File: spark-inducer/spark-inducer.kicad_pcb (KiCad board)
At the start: 2 copper layers, 233.3 x 128.5 mm, 100 parts, among them J1 Eurorack_Power_Header, J10 IO_A_1, J11 IO_A_3, J12 IO_A_2, J13 IO_A_4, J14 IO_B_1, J15 IO_B_3, J16 IO_B_2, J17 IO_B_4, J18 REF_SELECT, J19 POWER_A_1, J2 IO1, J20 POWER_A_2, J21 POWER_A_3, J22 POWER_A_4, J23 POWER_B_1, J24 POWER_B_2, J25 POWER_B_3, J26 POWER_B_4, J3 IO2, J4 IO3, J5 IO4, J6 IO5, J7 IO6, J8 OUT1, J9 OUT2, SW1 SWITCH, U1 TL072B, U2 TL072B, U3 TL431B, U4 L78LXX, U5 LM4040, U6 REF50XX

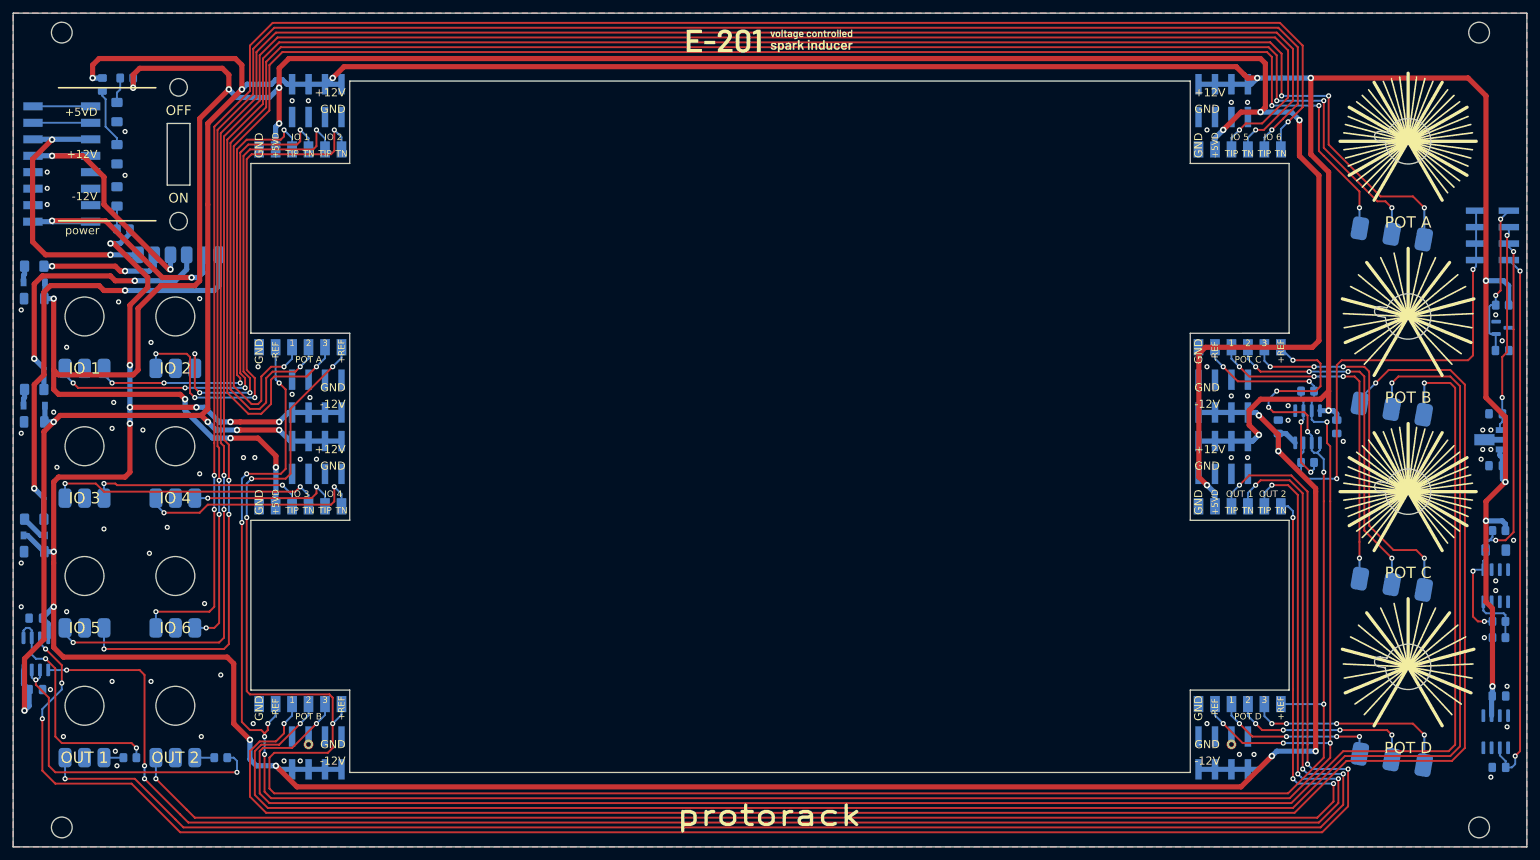
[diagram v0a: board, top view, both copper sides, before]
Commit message: Fix breadboard spacings, Add glue marks
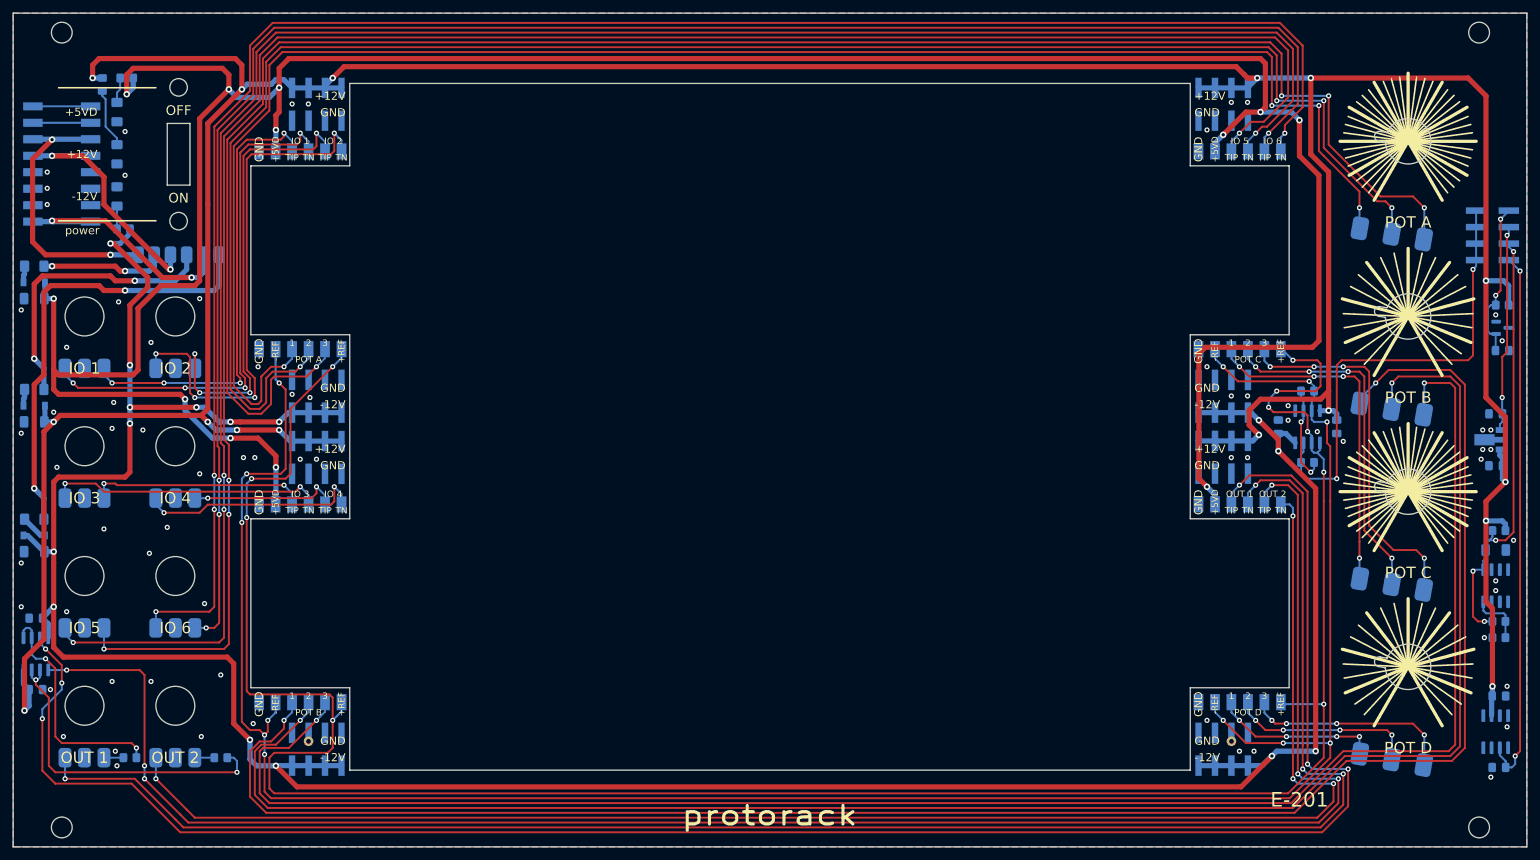
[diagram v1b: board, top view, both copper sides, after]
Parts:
- removed BREADBOARD_BOTTOM, BREADBOARD_TOP: Breadboard_MB-102, Protorack:Breadboard_MB-102
- removed Graphics: LOGO, Protorack2:Artwork_E-201
- added H23: BREADBOARD_TOP, Protorack:Breadboard_MB-102, F.Cu at (147.3, 75.3)
- added H24: BREADBOARD_BOT, Protorack:Breadboard_MB-102, F.Cu at (147.3, 129.7)
- added Logo: LOGO, Protorack2:Logo_28x6mm, F.Cu at (147.3, 162.8)
- moved J25 0.57 mm to (77.5, 152.2)
- moved J26 0.57 mm to (217.2, 152.2)
- moved J19 0.57 mm to (77.5, 52.8)
- moved J20 0.57 mm to (217.2, 52.8)
- moved TP1 0.49 mm to (76.2, 151.0)
- moved TP2 0.49 mm to (218.5, 151.0)
- moved J10 0.30 mm to (75.0, 66.4)
- moved J11 0.30 mm to (75.0, 84.2)
- moved J12 0.30 mm to (219.7, 66.4)
- moved J13 0.30 mm to (219.7, 84.2)
- moved J14 0.30 mm to (75.0, 120.8)
- moved J16 0.30 mm to (219.7, 120.8)
- moved J15 0.30 mm to (75.0, 138.6)
- moved J17 0.30 mm to (219.7, 138.6)
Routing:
- net +5V: track 430.9 -> 433.9 mm
- net -12V: track 433.3 -> 432.2 mm
- net +12V: track 593.9 -> 594.8 mm
- net /+REF: track 357.1 -> 356.3 mm
- net /IO_1_TN: track 81.4 -> 80.7 mm
- net /IO_1_T: track 71.3 -> 70.6 mm
- net /IO_2_TN: track 81.5 -> 80.8 mm
- net /IO_2_T: track 71.2 -> 70.5 mm
- net GND: vias 73 -> 71
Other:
- outline, holes or cut-outs redrawn
- board text added: "2022 Rev.2"
- board text added: "glue me up!"
- board text removed: "2021 Rev.1"

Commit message: Add new logos, Finalize silkscreen
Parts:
- removed the Logo at (147.3, 162.8)
- added Logo_protorack: Logo_protorack, Protorack:Logo_protorack, F.Cu at (147.3, 162.2)
- added Logo_spark_inducer: Logo_spark_inducer, Protorack:Logo_spark_inducer, F.Cu at (147.3, 43.8)
- moved QRCode 0.50 mm to (241.2, 161.5)
- renumbered REF** to TSKF
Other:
- board text added: "spark inducer"
- board text removed: "E-201"

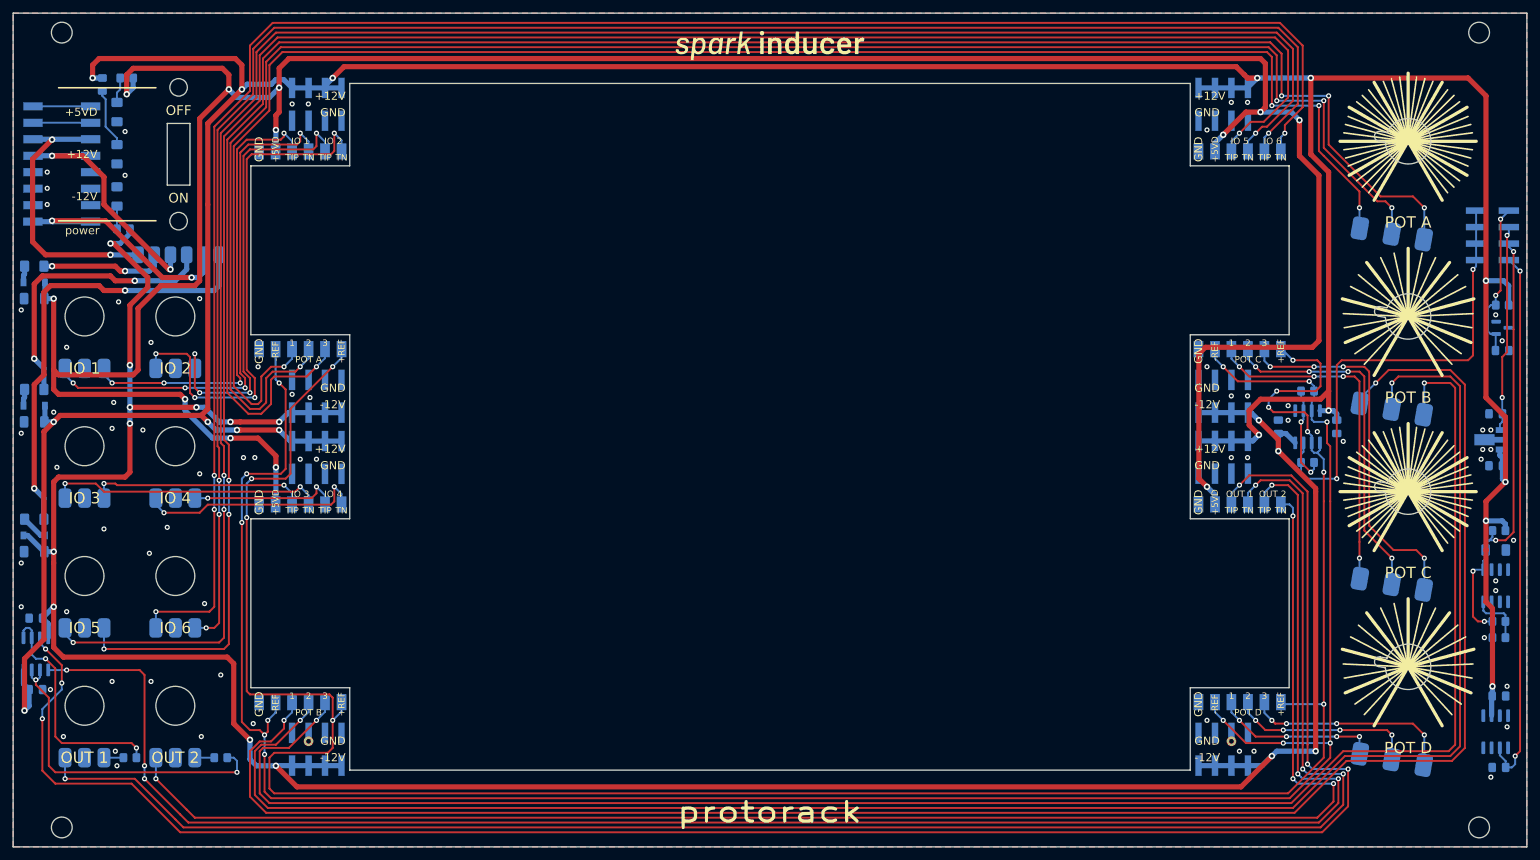
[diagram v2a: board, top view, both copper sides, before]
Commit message: Add knobs
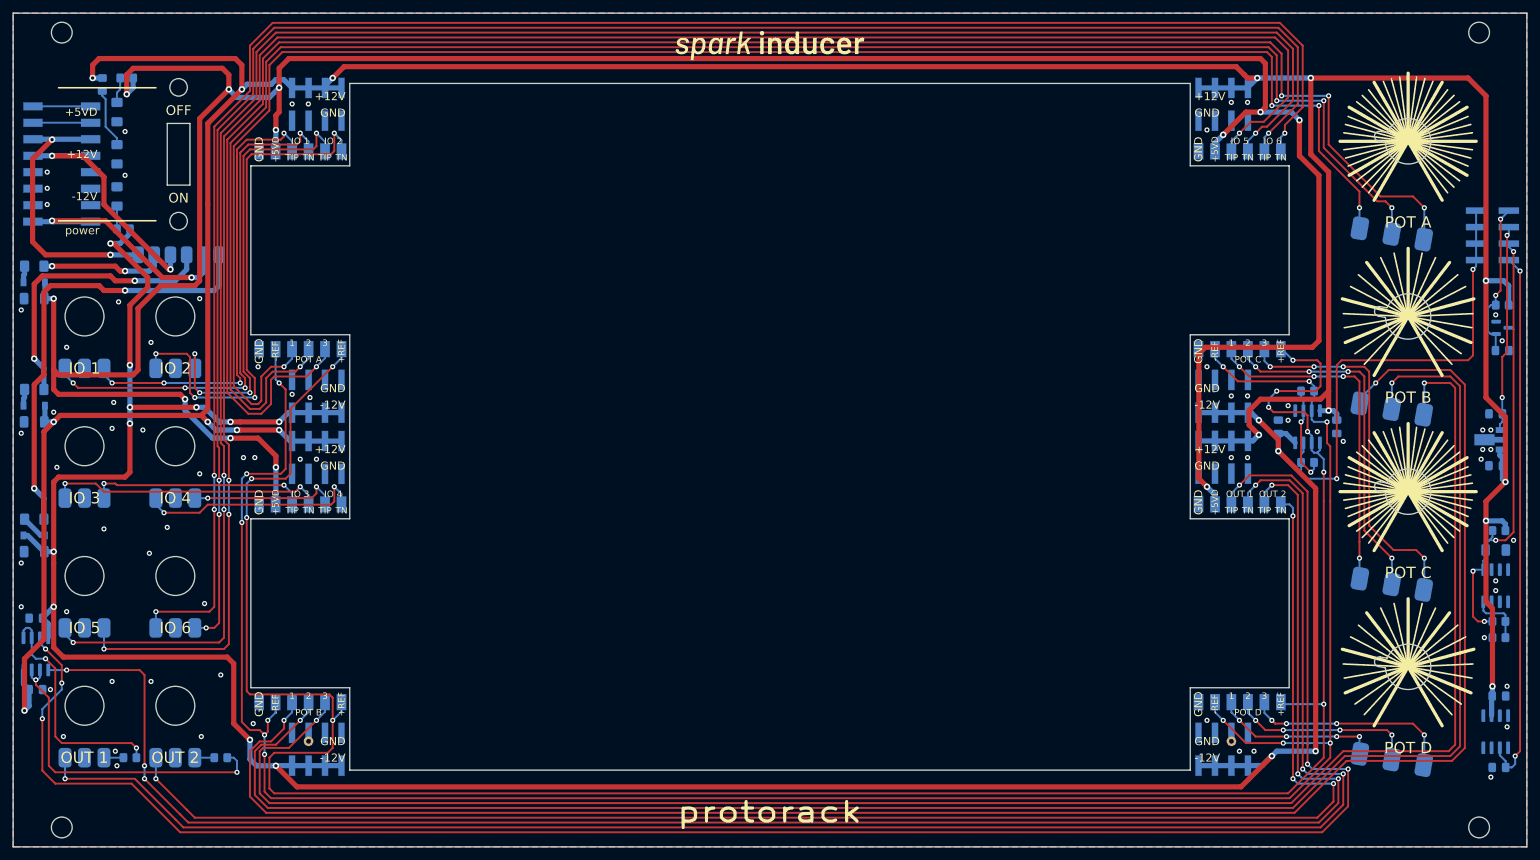
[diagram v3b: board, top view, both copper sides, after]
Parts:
- added H25: KNOB_POT_A, Protorack:Sifam_3-03-TPN130-006, F.Cu at (245.7, 58.5)
- added H26: KNOB_POT_B, Protorack:Sifam_3-03-TPN130-006, F.Cu at (245.7, 85.5)
- added H27: KNOB_POT_C, Protorack:Sifam_3-03-TPN130-006, F.Cu at (245.7, 112.5)
- added H28: KNOB_POT_D, Protorack:Sifam_3-03-TPN130-006, F.Cu at (245.7, 139.5)
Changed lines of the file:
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@@
     )
   )
+  (footprint "Protorack:Sifam_3-03-TPN130-006" (layer "F.Cu")
+    (at 245.7 85.5)
+    (property "Sheetfile" "spark.kicad_sch")
+    (property "Sheetname" "")
+    (fp_text reference "H26" (at 0 11 unlocked) (layer "F.Fab")
+      (effects (font (size 1 1) (thickness 0.15)))
+    )
+    (fp_text value "KNOB_POT_B" (at 0 -11 unlocked) (layer "F.Fab")
+      (effects (font (size 1 1) (thickness 0.15)))
+    )
+    (fp_rect (start -0.75 -7.5) (end 0.75 -0.5) (layer "Cmts.User") (width 0.12) (fill none))
+    (fp_arc (start 0.75 -6.5) (mid 0 6.543126) (end -0.75 -6.5) (layer "Cmts.User") (width 0.12))
+    (fp_circle (center 0 0) (end 9.5 0) (layer "Cmts.User") (width 0.12) (fill none))
+    (fp_line (start 10 10) (end 10 -10) (layer "F.CrtYd") (width 0.05))
+    (fp_line (start 10 -10) (end -10 -10) (layer "F.CrtYd") (width 0.05))
+    (fp_line (start -10 -10) (end -10 10) (layer "F.CrtYd") (width 0.05))
+    (fp_line (start -10 10) (end 10 10) (layer "F.CrtYd") (width 0.05))
+    (fp_rect (start -0.75 -7.5) (end 0.75 -0.5) (layer "F.Fab") (width 0.1) (fill none))
+    (fp_arc (start 0.75 -6.5) (mid 0 6.543126) (end -0.75 -6.5) (layer "F.Fab") (width 0.1))
+    (fp_circle (center 0 0) (end 9.5 0) (layer "F.Fab") (width 0.1) (fill none))
+    (model "${PROTORACK_3DMODEL_DIR}/Protorack.3dshapes/Knobs/Sifam_3-03-TPN130-006/Sifam_3-03-TPN130-006.wrl"
+      (offset (xyz 0 0 0.2))
+      (scale (xyz 1 1 1))
+      (rotate (xyz 0 0 180))
+    )
+  )
   (footprint "Protorack:Logo_spark_inducer" locked (layer "F.Cu")
     (at 147.35 43.75)
@@
     )
   )
+  (footprint "Protorack:Sifam_3-03-TPN130-006" (layer "F.Cu")
+    (at 245.7 58.5)
+    (property "Sheetfile" "spark.kicad_sch")
+    (property "Sheetname" "")
+    (fp_text reference "H25" (at 0 11 unlocked) (layer "F.Fab")
+      (effects (font (size 1 1) (thickness 0.15)))
+    )
+    (fp_text value "KNOB_POT_A" (at 0 -11 unlocked) (layer "F.Fab")
+      (effects (font (size 1 1) (thickness 0.15)))
+    )
+    (fp_rect (start -0.75 -7.5) (end 0.75 -0.5) (layer "Cmts.User") (width 0.12) (fill none))
+    (fp_arc (start 0.75 -6.5) (mid 0 6.543126) (end -0.75 -6.5) (layer "Cmts.User") (width 0.12))
+    (fp_circle (center 0 0) (end 9.5 0) (layer "Cmts.User") (width 0.12) (fill none))
+    (fp_line (start -10 10) (end 10 10) (layer "F.CrtYd") (width 0.05))
+    (fp_line (start 10 -10) (end -10 -10) (layer "F.CrtYd") (width 0.05))
+    (fp_line (start 10 10) (end 10 -10) (layer "F.CrtYd") (width 0.05))
+    (fp_line (start -10 -10) (end -10 10) (layer "F.CrtYd") (width 0.05))
+    (fp_rect (start -0.75 -7.5) (end 0.75 -0.5) (layer "F.Fab") (width 0.1) (fill none))
+    (fp_arc (start 0.75 -6.5) (mid 0 6.543126) (end -0.75 -6.5) (layer "F.Fab") (width 0.1))
+    (fp_circle (center 0 0) (end 9.5 0) (layer "F.Fab") (width 0.1) (fill none))
+    (model "${PROTORACK_3DMODEL_DIR}/Protorack.3dshapes/Knobs/Sifam_3-03-TPN130-006/Sifam_3-03-TPN130-006.wrl"
+      (offset (xyz 0 0 0.2))
+      (scale (xyz 1 1 1))
+      (rotate (xyz 0 0 180))
+    )
+  )
   (footprint "Protorack:Screw_ISO7380_M3x6" (layer "F.Cu")
     (at 38.2 41.75)
@@
       ) (layer "F.SilkS") (width 0) (fill solid))
   )
+  (footprint "Protorack:Sifam_3-03-TPN130-006" (layer "F.Cu")
+    (at 245.7 112.5)
+    (property "Sheetfile" "spark.kicad_sch")
+    (property "Sheetname" "")
+    (fp_text reference "H27" (at 0 11 unlocked) (layer "F.Fab")
+      (effects (font (size 1 1) (thickness 0.15)))
+    )
+    (fp_text value "KNOB_POT_C" (at 0 -11 unlocked) (layer "F.Fab")
+      (effects (font (size 1 1) (thickness 0.15)))
+    )
+    (fp_rect (start -0.75 -7.5) (end 0.75 -0.5) (layer "Cmts.User") (width 0.12) (fill none))
+    (fp_arc (start 0.75 -6.5) (mid 0 6.543126) (end -0.75 -6.5) (layer "Cmts.User") (width 0.12))
+    (fp_circle (center 0 0) (end 9.5 0) (layer "Cmts.User") (width 0.12) (fill none))
+    (fp_line (start 10 10) (end 10 -10) (layer "F.CrtYd") (width 0.05))
+    (fp_line (start -10 10) (end 10 10) (layer "F.CrtYd") (width 0.05))
+    (fp_line (start -10 -10) (end -10 10) (layer "F.CrtYd") (width 0.05))
+    (fp_line (start 10 -10) (end -10 -10) (layer "F.CrtYd") (width 0.05))
+    (fp_rect (start -0.75 -7.5) (end 0.75 -0.5) (layer "F.Fab") (width 0.1) (fill none))
+    (fp_arc (start 0.75 -6.5) (mid 0 6.543126) (end -0.75 -6.5) (layer "F.Fab") (width 0.1))
+    (fp_circle (center 0 0) (end 9.5 0) (layer "F.Fab") (width 0.1) (fill none))
+    (model "${PROTORACK_3DMODEL_DIR}/Protorack.3dshapes/Knobs/Sifam_3-03-TPN130-006/Sifam_3-03-TPN130-006.wrl"
+      (offset (xyz 0 0 0.2))
+      (scale (xyz 1 1 1))
+      (rotate (xyz 0 0 180))
+    )
+  )
   (footprint "Protorack:Nut_M6x2mm_Knurled" (layer "F.Cu")
     (at 41.7 105.5)
@@
     )
   )
+  (footprint "Protorack:Sifam_3-03-TPN130-006" (layer "F.Cu")
+    (at 245.7 139.5)
+    (property "Sheetfile" "spark.kicad_sch")
+    (property "Sheetname" "")
+    (fp_text reference "H28" (at 0 11 unlocked) (layer "F.Fab")
+      (effects (font (size 1 1) (thickness 0.15)))
+    )
+    (fp_text value "KNOB_POT_D" (at 0 -11 unlocked) (layer "F.Fab")
+      (effects (font (size 1 1) (thickness 0.15)))
+    )
+    (fp_rect (start -0.75 -7.5) (end 0.75 -0.5) (layer "Cmts.User") (width 0.12) (fill none))
+    (fp_arc (start 0.75 -6.5) (mid 0 6.543126) (end -0.75 -6.5) (layer "Cmts.User") (width 0.12))
+    (fp_circle (center 0 0) (end 9.5 0) (layer "Cmts.User") (width 0.12) (fill none))
+    (fp_line (start -10 10) (end 10 10) (layer "F.CrtYd") (width 0.05))
+    (fp_line (start -10 -10) (end -10 10) (layer "F.CrtYd") (width 0.05))
+    (fp_line (start 10 10) (end 10 -10) (layer "F.CrtYd") (width 0.05))
+    (fp_line (start 10 -10) (end -10 -10) (layer "F.CrtYd") (width 0.05))
+    (fp_rect (start -0.75 -7.5) (end 0.75 -0.5) (layer "F.Fab") (width 0.1) (fill none))
+    (fp_arc (start 0.75 -6.5) (mid 0 6.543126) (end -0.75 -6.5) (layer "F.Fab") (width 0.1))
+    (fp_circle (center 0 0) (end 9.5 0) (layer "F.Fab") (width 0.1) (fill none))
+    (model "${PROTORACK_3DMODEL_DIR}/Protorack.3dshapes/Knobs/Sifam_3-03-TPN130-006/Sifam_3-03-TPN130-006.wrl"
+      (offset (xyz 0 0 0.2))
+      (scale (xyz 1 1 1))
+      (rotate (xyz 0 0 180))
+    )
+  )
   (footprint "Protorack:Nut_M7x2mm_Black" (layer "F.Cu")
     (at 245.7 139.5)
@@
     (effects (font (size 1 1) (thickness 0.23)))
   )
-  (gr_text "+12V" (at 81.945 51.53) (layer "F.SilkS")
+  (gr_text "+12V" (at 81.945 51.59) (layer "F.SilkS")
     (effects (font (size 1.25 1.25) (thickness 0.25)) (justify right))
   )
-  (gr_text "GND" (at 81.945 54.07) (layer "F.SilkS")
+  (gr_text "GND" (at 81.945 54.13) (layer "F.SilkS")
     (effects (font (size 1.25 1.25) (thickness 0.25)) (justify right))
   )
@@
     (effects (font (size 1 1) (thickness 0.2)))
   )
-  (gr_text "GND" (at 81.945 96.53) (layer "F.SilkS")
+  (gr_text "GND" (at 81.945 96.59) (layer "F.SilkS")
     (effects (font (size 1.25 1.25) (thickness 0.25)) (justify right))
   )
-  (gr_text "-12V" (at 81.945 99.07) (layer "F.SilkS")
+  (gr_text "-12V" (at 81.945 99.13) (layer "F.SilkS")
     (effects (font (size 1.25 1.25) (thickness 0.25)) (justify right))
   )
@@
     (effects (font (size 1 1) (thickness 0.23)))
   )
-  (gr_text "GND" (at 81.945 150.93) (layer "F.SilkS")
+  (gr_text "GND" (at 81.945 150.99) (layer "F.SilkS")
     (effects (font (size 1.25 1.25) (thickness 0.25)) (justify right))
   )
-  (gr_text "-12V" (at 81.945 153.47) (layer "F.SilkS")
+  (gr_text "-12V" (at 81.945 153.53) (layer "F.SilkS")
     (effects (font (size 1.25 1.25) (thickness 0.25)) (justify right))
   )
-  (gr_text "GND" (at 81.945 108.47) (layer "F.SilkS")
+  (gr_text "GND" (at 81.945 108.53) (layer "F.SilkS")
     (effects (font (size 1.25 1.25) (thickness 0.25)) (justify right))
   )
-  (gr_text "+12V" (at 81.945 105.93) (layer "F.SilkS")
+  (gr_text "+12V" (at 81.945 105.99) (layer "F.SilkS")
     (effects (font (size 1.25 1.25) (thickness 0.25)) (justify right))
   )
@@
     (effects (font (size 1.25 1.25) (thickness 0.25)))
   )
-  (gr_text "+12V" (at 212.755 105.93) (layer "F.SilkS")
+  (gr_text "+12V" (at 212.755 105.99) (layer "F.SilkS")
     (effects (font (size 1.25 1.25) (thickness 0.25)) (justify left))
   )
-  (gr_text "GND" (at 212.755 108.47) (layer "F.SilkS")
+  (gr_text "GND" (at 212.755 108.53) (layer "F.SilkS")
     (effects (font (size 1.25 1.25) (thickness 0.25)) (justify left))
   )
-  (gr_text "-12V" (at 212.755 99.07) (layer "F.SilkS")
+  (gr_text "-12V" (at 212.755 99.13) (layer "F.SilkS")
     (effects (font (size 1.25 1.25) (thickness 0.25)) (justify left))
   )
-  (gr_text "GND" (at 212.755 96.53) (layer "F.SilkS")
+  (gr_text "GND" (at 212.755 96.59) (layer "F.SilkS")
     (effects (font (size 1.25 1.25) (thickness 0.25)) (justify left))
   )
@@
     (effects (font (size 1 1) (thickness 0.2)))
   )
-  (gr_text "GND" (at 212.755 150.93) (layer "F.SilkS")
+  (gr_text "GND" (at 212.755 150.99) (layer "F.SilkS")
     (effects (font (size 1.25 1.25) (thickness 0.25)) (justify left))
   )
-  (gr_text "-12V" (at 212.755 153.47) (layer "F.SilkS")
+  (gr_text "-12V" (at 212.755 153.53) (layer "F.SilkS")
     (effects (font (size 1.25 1.25) (thickness 0.25)) (justify left))
   )
@@
     (effects (font (size 1.25 1.25) (thickness 0.25)))
   )
-  (gr_text "+12V" (at 212.755 51.53) (layer "F.SilkS")
+  (gr_text "+12V" (at 212.755 51.59) (layer "F.SilkS")
     (effects (font (size 1.25 1.25) (thickness 0.25)) (justify left))
   )
-  (gr_text "GND" (at 212.755 54.07) (layer "F.SilkS")
+  (gr_text "GND" (at 212.755 54.13) (layer "F.SilkS")
     (effects (font (size 1.25 1.25) (thickness 0.25)) (justify left))
   )

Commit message: Update qr code
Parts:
- QRCode: footprint Protorack2:QRCode_E-201 -> Protorack:QRCode_spark-inducer
